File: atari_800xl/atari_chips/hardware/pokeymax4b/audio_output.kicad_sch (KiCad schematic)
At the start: 17 parts, among them U1 TSV854IQ4T

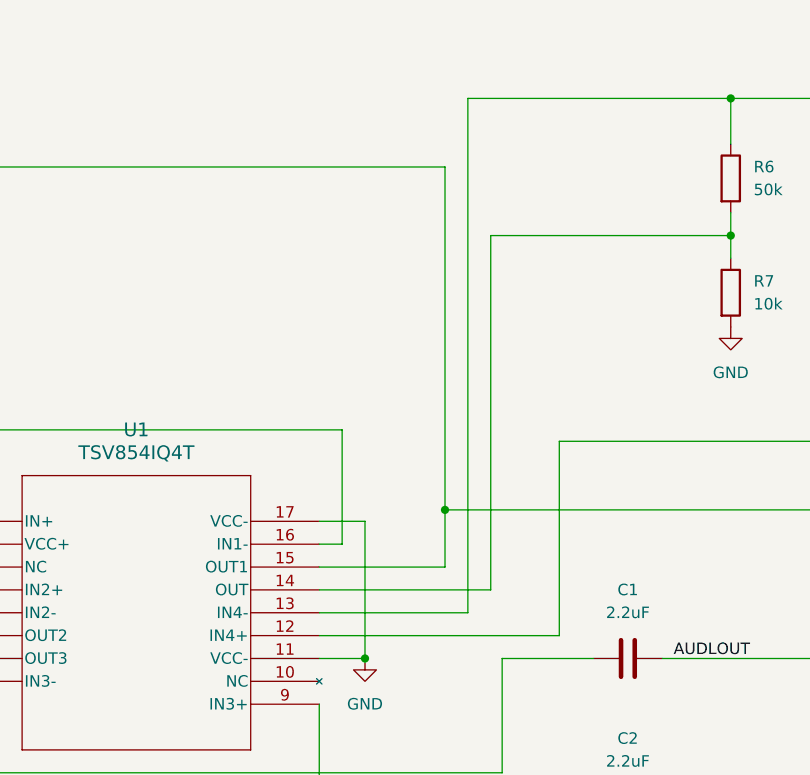
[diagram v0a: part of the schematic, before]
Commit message: After testing 4b first run, there are a few issues. Updated to 4b2 with: Corrected L/R output. ADC bias improvement. ADC preamp out/in- corrected. Moved silkscreen name!
git-svn-id: svn+ssh://192.168.0.3/home/svnfpga/repo/trunk@1475 d6161ac3-aae1-4d52-9b05-ea9ac36b53d3
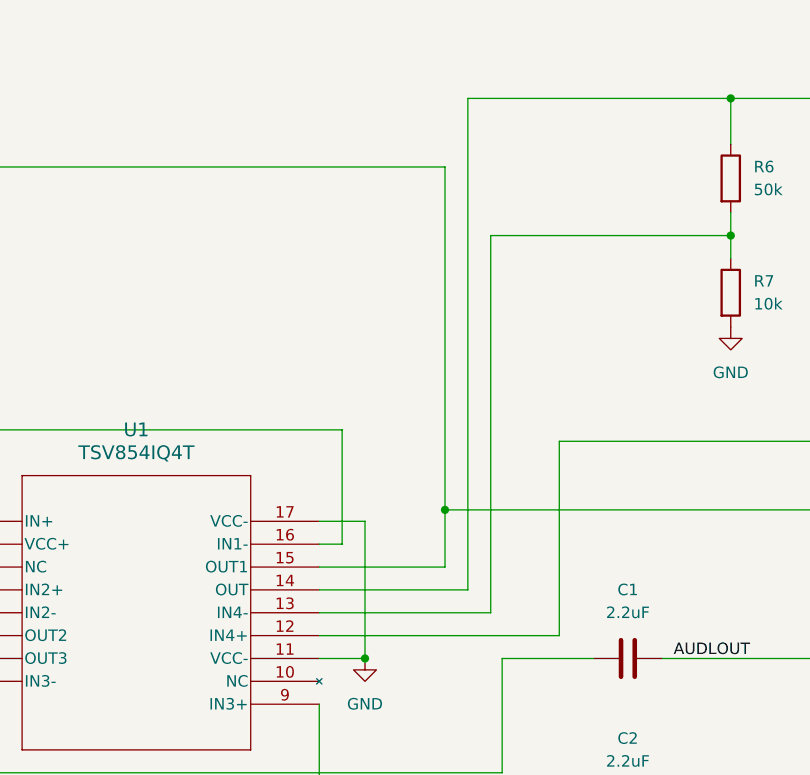
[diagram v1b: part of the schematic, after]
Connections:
- net AUD_IN_AMP: now also U1.14 (OUT); no longer U1.13 (IN4-)
- net at R6.2, R7.1: now also U1.13 (IN4-); no longer U1.14 (OUT)
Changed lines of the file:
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@@
 	(wire
 		(pts
-			(xy 173.99 57.15) (xy 173.99 114.3)
-		)
-		(stroke
-			(width 0)
-			(type default)
-		)
-	)
-	(wire
-		(pts
-			(xy 176.53 72.39) (xy 176.53 111.76)
+			(xy 173.99 57.15) (xy 173.99 111.76)
+		)
+		(stroke
+			(width 0)
+			(type default)
+		)
+	)
+	(wire
+		(pts
+			(xy 176.53 72.39) (xy 176.53 114.3)
 		)
 		(stroke
@@
 	(wire
 		(pts
+			(xy 157.48 114.3) (xy 176.53 114.3)
+		)
+		(stroke
+			(width 0)
+			(type default)
+		)
+	)
+	(wire
+		(pts
 			(xy 43.18 114.3) (xy 49.53 114.3)
 		)
@@
 	(wire
 		(pts
-			(xy 157.48 114.3) (xy 173.99 114.3)
-		)
-		(stroke
-			(width 0)
-			(type default)
-		)
-	)
-	(wire
-		(pts
 			(xy 203.2 69.85) (xy 203.2 72.39)
 		)
@@
 	(wire
 		(pts
-			(xy 157.48 111.76) (xy 176.53 111.76)
-		)
-		(stroke
-			(width 0)
-			(type default)
-		)
-	)
-	(wire
-		(pts
 			(xy 195.58 119.38) (xy 261.62 119.38)
 		)
@@
 		)
 		(stroke
+			(width 0)
+			(type default)
+		)
+	)
+	(wire
+		(pts
+			(xy 157.48 111.76) (xy 173.99 111.76)
+		)
+		(stroke
